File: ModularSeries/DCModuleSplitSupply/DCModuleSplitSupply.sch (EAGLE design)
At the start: 21 parts

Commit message: All PCBs now use unified library, Eagle library added
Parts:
- DCDC1: device ElectricNoodleBox2018:VRA1212ZP-6WR3 -> ElectricNoodleBox:VRA1212ZP-6WR3
- J1, J6, J7: value (none) -> 2XMOLEX; device SparkFun-Connectors:CONN_02POLAR -> ElectricNoodleBox:2XMOLEX
- J2, J3, J4, J5, J8: value (none) -> 4XMOLEX; device SparkFun-Connectors:CONN_04POLAR -> ElectricNoodleBox:4XMOLEX
- PREF1, PREF2: device ElectricNoodleBox2018:LM4040_TO92 -> ElectricNoodleBox:LM4040_TO92
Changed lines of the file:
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@@
 </classes>
 <parts>
-<part name="DCDC1" library="ElectricNoodleBox2018" deviceset="VRA1212ZP-6WR3" device="" value="+/- 12V"/>
+<part name="DCDC1" library="ElectricNoodleBox" deviceset="VRA1212ZP-6WR3" device="" value="+/- 12V"/>
 <part name="C1" library="rcl" library_urn="urn:adsk.eagle:library:334" deviceset="CPOL-EU" device="E2.5-6" package3d_urn="urn:adsk.eagle:package:23349/1" value="100µF"/>
 <part name="C2" library="rcl" library_urn="urn:adsk.eagle:library:334" deviceset="CPOL-EU" device="E2-5" package3d_urn="urn:adsk.eagle:package:23346/2" value="10µF"/>
 <part name="C3" library="rcl" library_urn="urn:adsk.eagle:library:334" deviceset="CPOL-EU" device="E2-5" package3d_urn="urn:adsk.eagle:package:23346/2" value="10µF"/>
-<part name="PREF1" library="ElectricNoodleBox2018" deviceset="LM4040_TO92" device="" value="LM4040 10V"/>
-<part name="PREF2" library="ElectricNoodleBox2018" deviceset="LM4040_TO92" device="" value="LM4040 10V"/>
+<part name="PREF1" library="ElectricNoodleBox" deviceset="LM4040_TO92" device="" value="LM4040 10V"/>
+<part name="PREF2" library="ElectricNoodleBox" deviceset="LM4040_TO92" device="" value="LM4040 10V"/>
 <part name="P+1" library="supply1" library_urn="urn:adsk.eagle:library:371" deviceset="+12V" device=""/>
 <part name="P-1" library="supply1" library_urn="urn:adsk.eagle:library:371" deviceset="-12V" device=""/>
@@
 <part name="R2" library="rcl" library_urn="urn:adsk.eagle:library:334" deviceset="R-EU_" device="0207/10" package3d_urn="urn:adsk.eagle:package:23491/2" value="4K7"/>
 <part name="AGND1" library="supply1" library_urn="urn:adsk.eagle:library:371" deviceset="AGND" device=""/>
-<part name="J1" library="SparkFun-Connectors" deviceset="CONN_02" device="POLAR"/>
-<part name="J2" library="SparkFun-Connectors" deviceset="CONN_04" device="POLAR"/>
-<part name="J3" library="SparkFun-Connectors" deviceset="CONN_04" device="POLAR"/>
-<part name="J4" library="SparkFun-Connectors" deviceset="CONN_04" device="POLAR"/>
-<part name="J5" library="SparkFun-Connectors" deviceset="CONN_04" device="POLAR"/>
-<part name="J6" library="SparkFun-Connectors" deviceset="CONN_02" device="POLAR"/>
-<part name="J7" library="SparkFun-Connectors" deviceset="CONN_02" device="POLAR"/>
-<part name="J8" library="SparkFun-Connectors" deviceset="CONN_04" device="POLAR"/>
+<part name="J1" library="ElectricNoodleBox" deviceset="2XMOLEX" device=""/>
+<part name="J2" library="ElectricNoodleBox" deviceset="4XMOLEX" device=""/>
+<part name="J3" library="ElectricNoodleBox" deviceset="4XMOLEX" device=""/>
+<part name="J4" library="ElectricNoodleBox" deviceset="4XMOLEX" device=""/>
+<part name="J5" library="ElectricNoodleBox" deviceset="4XMOLEX" device=""/>
+<part name="J6" library="ElectricNoodleBox" deviceset="2XMOLEX" device=""/>
+<part name="J7" library="ElectricNoodleBox" deviceset="2XMOLEX" device=""/>
+<part name="J8" library="ElectricNoodleBox" deviceset="4XMOLEX" device=""/>
 <part name="P-2" library="supply1" library_urn="urn:adsk.eagle:library:371" deviceset="-12V" device=""/>
 <part name="P+2" library="supply1" library_urn="urn:adsk.eagle:library:371" deviceset="+12V" device=""/>
@@
 </instance>
 <instance part="J1" gate="G$1" x="25.4" y="45.72" smashed="yes" rot="MR180">
-<attribute name="VALUE" x="22.86" y="50.546" size="1.778" layer="96" font="vector" rot="MR180"/>
 <attribute name="NAME" x="22.86" y="40.132" size="1.778" layer="95" font="vector" rot="MR180"/>
 </instance>
 <instance part="J2" gate="G$1" x="121.92" y="73.66" smashed="yes" rot="MR180">
-<attribute name="VALUE" x="116.84" y="81.026" size="1.778" layer="96" font="vector" rot="MR180"/>
 <attribute name="NAME" x="116.84" y="65.532" size="1.778" layer="95" font="vector" rot="MR180"/>
 </instance>
 <instance part="J3" gate="G$1" x="121.92" y="58.42" smashed="yes" rot="MR180">
-<attribute name="VALUE" x="116.84" y="65.786" size="1.778" layer="96" font="vector" rot="MR180"/>
 <attribute name="NAME" x="116.84" y="50.292" size="1.778" layer="95" font="vector" rot="MR180"/>
 </instance>
 <instance part="J4" gate="G$1" x="121.92" y="43.18" smashed="yes" rot="MR180">
-<attribute name="VALUE" x="116.84" y="50.546" size="1.778" layer="96" font="vector" rot="MR180"/>
 <attribute name="NAME" x="116.84" y="35.052" size="1.778" layer="95" font="vector" rot="MR180"/>
 </instance>
 <instance part="J5" gate="G$1" x="121.92" y="27.94" smashed="yes" rot="MR180">
-<attribute name="VALUE" x="116.84" y="35.306" size="1.778" layer="96" font="vector" rot="MR180"/>
 <attribute name="NAME" x="116.84" y="19.812" size="1.778" layer="95" font="vector" rot="MR180"/>
 </instance>
 <instance part="J6" gate="G$1" x="154.94" y="48.26" smashed="yes" rot="R180">
-<attribute name="VALUE" x="157.48" y="53.086" size="1.778" layer="96" font="vector" rot="R180"/>
 <attribute name="NAME" x="157.48" y="42.672" size="1.778" layer="95" font="vector" rot="R180"/>
 </instance>
 <instance part="J7" gate="G$1" x="154.94" y="35.56" smashed="yes" rot="R180">
-<attribute name="VALUE" x="157.48" y="40.386" size="1.778" layer="96" font="vector" rot="R180"/>
 <attribute name="NAME" x="157.48" y="29.972" size="1.778" layer="95" font="vector" rot="R180"/>
 </instance>
 <instance part="J8" gate="G$1" x="121.92" y="12.7" smashed="yes" rot="MR180">
-<attribute name="VALUE" x="116.84" y="20.066" size="1.778" layer="96" font="vector" rot="MR180"/>
 <attribute name="NAME" x="116.84" y="4.572" size="1.778" layer="95" font="vector" rot="MR180"/>
 </instance>

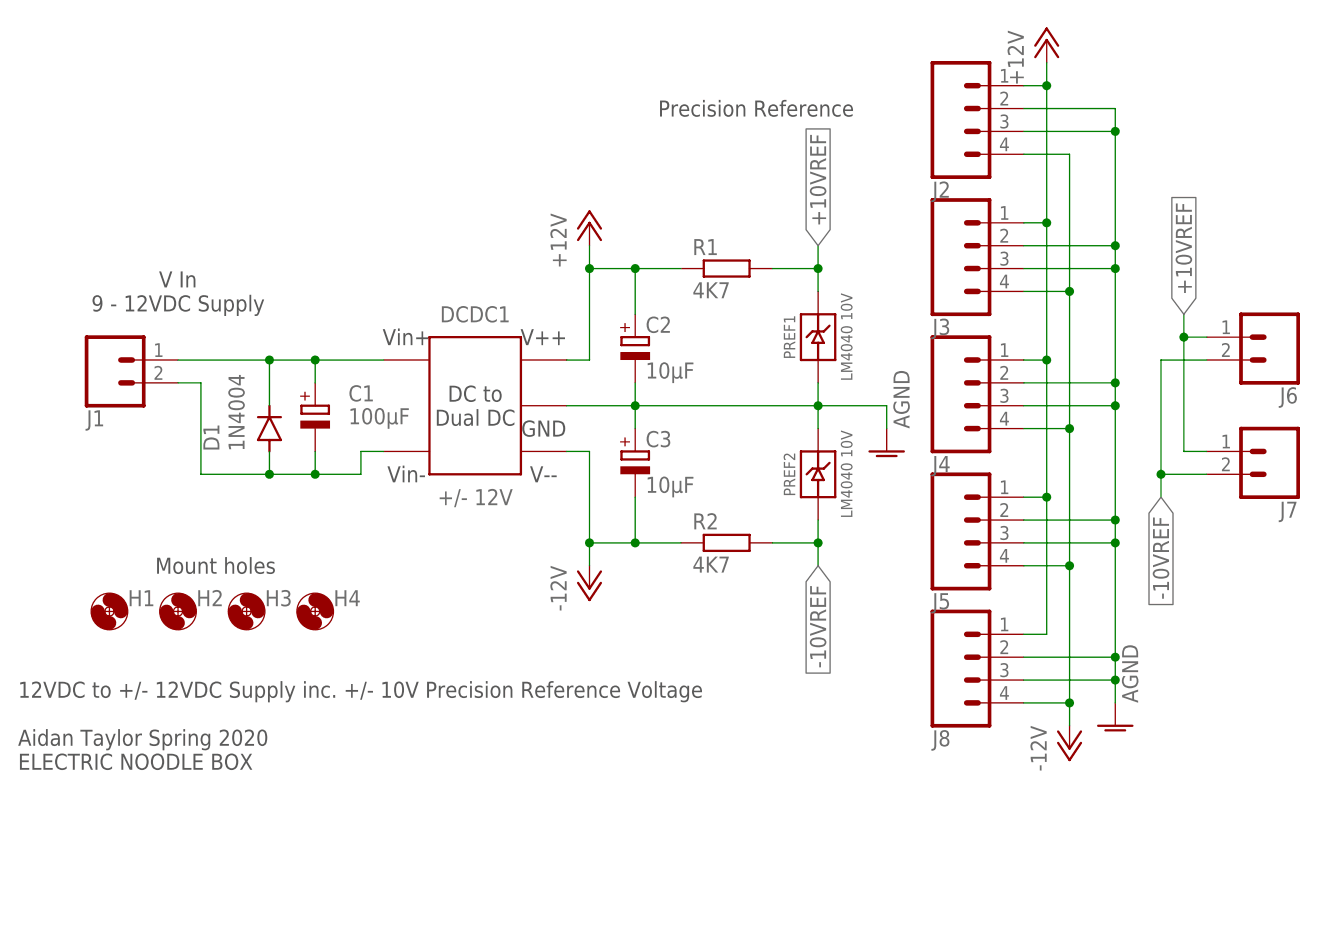
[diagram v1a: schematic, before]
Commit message: Updates to Prism, VCA, PSU and Prism BOM added
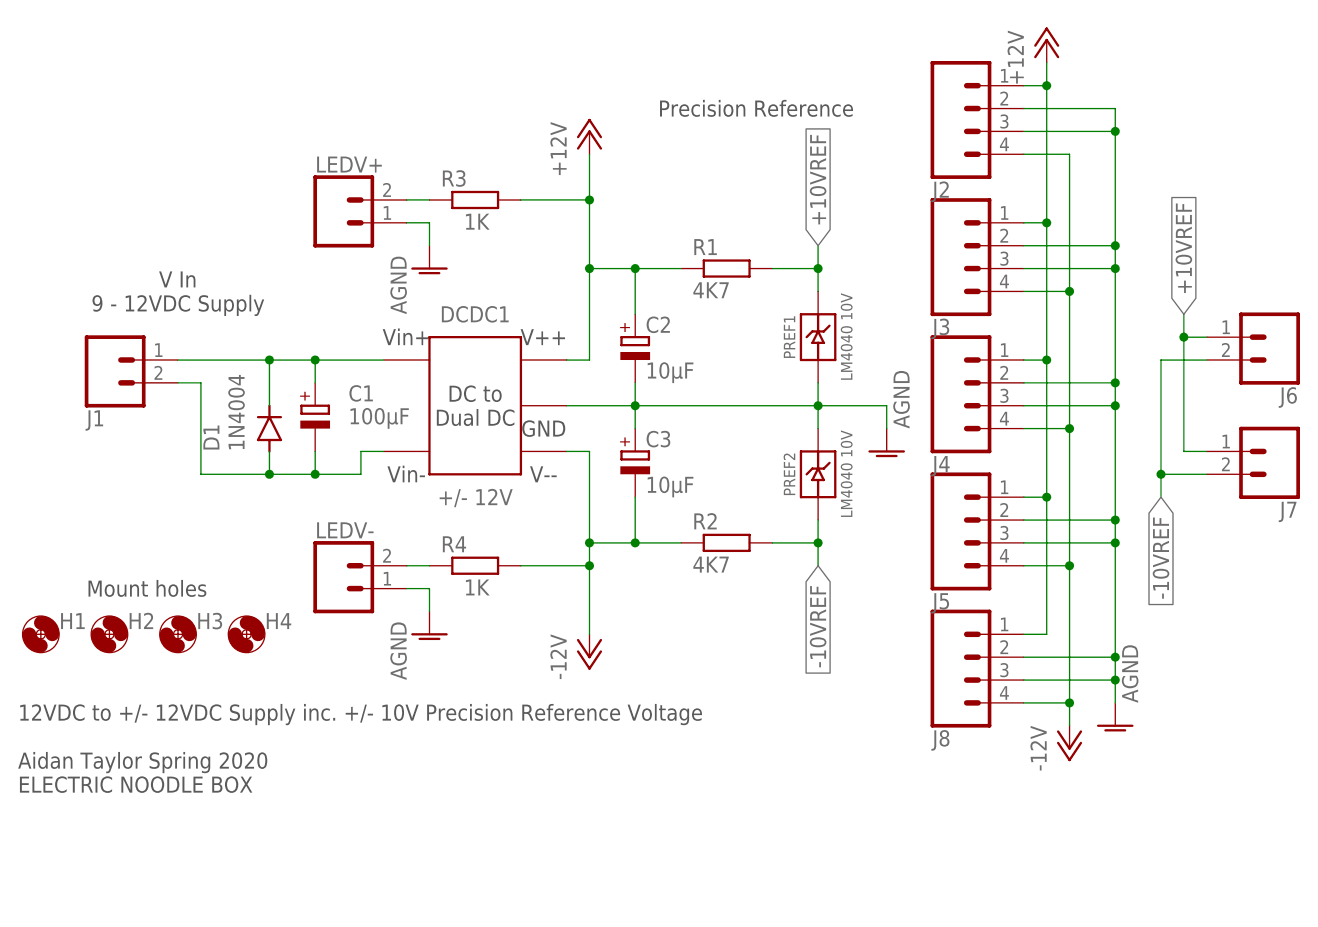
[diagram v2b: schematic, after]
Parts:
- added LEDV+, LEDV-: 2XWIREPAD, ElectricNoodleBox:2XWIREPAD
- added R3, R4: 1K, rcl:R-EU_0207/10
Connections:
- new net N$2: LEDV+.2, R3.1
- new net N$3: LEDV-.2, R4.1
- net +12V: now also R3.2
- net -12V: now also R4.2
- net AGND: now also LEDV+.1, LEDV-.1
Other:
- moved on the sheet: H1, H2, H3, H4
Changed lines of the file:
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@@
 <part name="H3" library="holes" library_urn="urn:adsk.eagle:library:237" deviceset="MOUNT-HOLE" device="3.2" package3d_urn="urn:adsk.eagle:package:14275/1"/>
 <part name="H4" library="holes" library_urn="urn:adsk.eagle:library:237" deviceset="MOUNT-HOLE" device="3.2" package3d_urn="urn:adsk.eagle:package:14275/1"/>
+<part name="LEDV+" library="ElectricNoodleBox" deviceset="2XWIREPAD" device=""/>
+<part name="LEDV-" library="ElectricNoodleBox" deviceset="2XWIREPAD" device=""/>
+<part name="R3" library="rcl" library_urn="urn:adsk.eagle:library:334" deviceset="R-EU_" device="0207/10" package3d_urn="urn:adsk.eagle:package:23491/2" value="1K"/>
+<part name="AGND3" library="supply1" library_urn="urn:adsk.eagle:library:371" deviceset="AGND" device=""/>
+<part name="AGND4" library="supply1" library_urn="urn:adsk.eagle:library:371" deviceset="AGND" device=""/>
+<part name="R4" library="rcl" library_urn="urn:adsk.eagle:library:334" deviceset="R-EU_" device="0207/10" package3d_urn="urn:adsk.eagle:package:23491/2" value="1K"/>
 </parts>
 <sheets>
@@
 <text x="33.02" y="53.34" size="1.778" layer="97" align="center">V In
 9 - 12VDC Supply</text>
-<text x="15.24" y="5.08" size="1.778" layer="97" align="center-left">12VDC to +/- 12VDC Supply inc. +/- 10V Precision Reference Voltage
+<text x="15.24" y="2.54" size="1.778" layer="97" align="center-left">12VDC to +/- 12VDC Supply inc. +/- 10V Precision Reference Voltage
 Aidan Taylor Spring 2020
 ELECTRIC NOODLE BOX</text>
 <text x="86.36" y="73.66" size="1.778" layer="97" align="center-left">Precision Reference</text>
-<text x="30.48" y="22.86" size="1.778" layer="97" align="center-left">Mount holes</text>
+<text x="22.86" y="20.32" size="1.778" layer="97" align="center-left">Mount holes</text>
 </plain>
 <instances>
@@
 <attribute name="VALUE" x="107.315" y="33.02" size="1.27" layer="96" rot="R90" align="center"/>
 </instance>
-<instance part="P+1" gate="1" x="78.74" y="60.96" smashed="yes">
-<attribute name="VALUE" x="76.2" y="55.88" size="1.778" layer="96" rot="R90"/>
-</instance>
-<instance part="P-1" gate="1" x="78.74" y="20.32" smashed="yes">
-<attribute name="VALUE" x="76.2" y="17.78" size="1.778" layer="96" rot="R90"/>
+<instance part="P+1" gate="1" x="78.74" y="71.12" smashed="yes">
+<attribute name="VALUE" x="76.2" y="66.04" size="1.778" layer="96" rot="R90"/>
+</instance>
+<instance part="P-1" gate="1" x="78.74" y="12.7" smashed="yes">
+<attribute name="VALUE" x="76.2" y="10.16" size="1.778" layer="96" rot="R90"/>
 </instance>
 <instance part="R1" gate="G$1" x="93.98" y="55.88" smashed="yes">
@@
 <attribute name="VALUE" x="40.4114" y="35.56" size="1.778" layer="96" rot="R90"/>
 </instance>
-<instance part="H1" gate="G$1" x="25.4" y="17.78" smashed="yes">
-<attribute name="NAME" x="27.432" y="18.3642" size="1.778" layer="95"/>
-</instance>
-<instance part="H2" gate="G$1" x="33.02" y="17.78" smashed="yes">
-<attribute name="NAME" x="35.052" y="18.3642" size="1.778" layer="95"/>
-</instance>
-<instance part="H3" gate="G$1" x="40.64" y="17.78" smashed="yes">
-<attribute name="NAME" x="42.672" y="18.3642" size="1.778" layer="95"/>
-</instance>
-<instance part="H4" gate="G$1" x="48.26" y="17.78" smashed="yes">
-<attribute name="NAME" x="50.292" y="18.3642" size="1.778" layer="95"/>
+<instance part="H1" gate="G$1" x="17.78" y="15.24" smashed="yes">
+<attribute name="NAME" x="19.812" y="15.8242" size="1.778" layer="95"/>
+</instance>
+<instance part="H2" gate="G$1" x="25.4" y="15.24" smashed="yes">
+<attribute name="NAME" x="27.432" y="15.8242" size="1.778" layer="95"/>
+</instance>
+<instance part="H3" gate="G$1" x="33.02" y="15.24" smashed="yes">
+<attribute name="NAME" x="35.052" y="15.8242" size="1.778" layer="95"/>
+</instance>
+<instance part="H4" gate="G$1" x="40.64" y="15.24" smashed="yes">
+<attribute name="NAME" x="42.672" y="15.8242" size="1.778" layer="95"/>
+</instance>
+<instance part="LEDV+" gate="G$1" x="50.8" y="60.96" smashed="yes">
+<attribute name="NAME" x="48.26" y="66.548" size="1.778" layer="95" font="vector"/>
+</instance>
+<instance part="LEDV-" gate="G$1" x="50.8" y="20.32" smashed="yes">
+<attribute name="NAME" x="48.26" y="25.908" size="1.778" layer="95" font="vector"/>
+</instance>
+<instance part="R3" gate="G$1" x="66.04" y="63.5" smashed="yes">
+<attribute name="NAME" x="62.23" y="64.9986" size="1.778" layer="95"/>
+<attribute name="VALUE" x="64.77" y="60.198" size="1.778" layer="96"/>
+</instance>
+<instance part="AGND3" gate="VR1" x="60.96" y="55.88" smashed="yes">
+<attribute name="VALUE" x="58.42" y="50.8" size="1.778" layer="96" rot="R90"/>
+</instance>
+<instance part="AGND4" gate="VR1" x="60.96" y="15.24" smashed="yes">
+<attribute name="VALUE" x="58.42" y="10.16" size="1.778" layer="96" rot="R90"/>
+</instance>
+<instance part="R4" gate="G$1" x="66.04" y="22.86" smashed="yes">
+<attribute name="NAME" x="62.23" y="24.3586" size="1.778" layer="95"/>
+<attribute name="VALUE" x="64.77" y="19.558" size="1.778" layer="96"/>
 </instance>
 </instances>
@@
 <wire x1="78.74" y1="45.72" x2="78.74" y2="55.88" width="0.1524" layer="91"/>
 <pinref part="R1" gate="G$1" pin="1"/>
-<wire x1="78.74" y1="55.88" x2="78.74" y2="58.42" width="0.1524" layer="91"/>
+<wire x1="78.74" y1="55.88" x2="78.74" y2="63.5" width="0.1524" layer="91"/>
+<wire x1="78.74" y1="63.5" x2="78.74" y2="68.58" width="0.1524" layer="91"/>
 <wire x1="78.74" y1="55.88" x2="83.82" y2="55.88" width="0.1524" layer="91"/>
 <junction x="78.74" y="55.88"/>
@@
 <wire x1="83.82" y1="55.88" x2="83.82" y2="50.8" width="0.1524" layer="91"/>
 <junction x="83.82" y="55.88"/>
+<pinref part="R3" gate="G$1" pin="2"/>
+<wire x1="71.12" y1="63.5" x2="78.74" y2="63.5" width="0.1524" layer="91"/>
+<junction x="78.74" y="63.5"/>
 </segment>
 <segment>
@@
 <pinref part="C3" gate="G$1" pin="-"/>
 <wire x1="78.74" y1="25.4" x2="78.74" y2="22.86" width="0.1524" layer="91"/>
+<wire x1="78.74" y1="22.86" x2="78.74" y2="15.24" width="0.1524" layer="91"/>
 <wire x1="83.82" y1="30.48" x2="83.82" y2="25.4" width="0.1524" layer="91"/>
 <pinref part="R2" gate="G$1" pin="1"/>
@@
 <junction x="78.74" y="25.4"/>
 <junction x="83.82" y="25.4"/>
+<pinref part="R4" gate="G$1" pin="2"/>
+<wire x1="71.12" y1="22.86" x2="78.74" y2="22.86" width="0.1524" layer="91"/>
+<junction x="78.74" y="22.86"/>
 </segment>
 <segment>
@@
 <junction x="137.16" y="10.16"/>
 </segment>
-</net>
+<segment>
+<pinref part="LEDV+" gate="G$1" pin="1"/>
+<wire x1="58.42" y1="60.96" x2="60.96" y2="60.96" width="0.1524" layer="91"/>
+<pinref part="AGND3" gate="VR1" pin="AGND"/>
+<wire x1="60.96" y1="60.96" x2="60.96" y2="58.42" width="0.1524" layer="91"/>
+</segment>
+<segment>
+<pinref part="LEDV-" gate="G$1" pin="1"/>
+<wire x1="58.42" y1="20.32" x2="60.96" y2="20.32" width="0.1524" layer="91"/>
+<pinref part="AGND4" gate="VR1" pin="AGND"/>
+<wire x1="60.96" y1="20.32" x2="60.96" y2="17.78" width="0.1524" layer="91"/>
+</segment>
+</net>
+<net name="N$2" class="0">
+<segment>
+<pinref part="LEDV+" gate="G$1" pin="2"/>
+<pinref part="R3" gate="G$1" pin="1"/>
+<wire x1="58.42" y1="63.5" x2="60.96" y2="63.5" width="0.1524" layer="91"/>
+</segment>
+</net>
+<net name="N$3" class="0">
+<segment>
+<pinref part="LEDV-" gate="G$1" pin="2"/>
+<pinref part="R4" gate="G$1" pin="1"/>
+<wire x1="58.42" y1="22.86" x2="60.96" y2="22.86" width="0.1524" layer="91"/>
+</segment>
+</net>

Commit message: Portals files updated, schematic exports and images included
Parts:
- added LINK: 2XWIREPAD, ElectricNoodleBox:2XWIREPAD
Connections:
- net AGND: now also LINK.1, LINK.2
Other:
- note added: "Ground link for Banana systems"
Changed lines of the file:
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@@
 <part name="AGND4" library="supply1" library_urn="urn:adsk.eagle:library:371" deviceset="AGND" device=""/>
 <part name="R4" library="rcl" library_urn="urn:adsk.eagle:library:334" deviceset="R-EU_" device="0207/10" package3d_urn="urn:adsk.eagle:package:23491/2" value="1K"/>
+<part name="LINK" library="ElectricNoodleBox" deviceset="2XWIREPAD" device=""/>
+<part name="AGND5" library="supply1" library_urn="urn:adsk.eagle:library:371" deviceset="AGND" device=""/>
 </parts>
 <sheets>
@@
 <text x="86.36" y="73.66" size="1.778" layer="97" align="center-left">Precision Reference</text>
 <text x="22.86" y="20.32" size="1.778" layer="97" align="center-left">Mount holes</text>
+<text x="22.86" y="76.2" size="1.778" layer="91">Ground link
+for Banana systems</text>
 </plain>
 <instances>
@@
 <attribute name="NAME" x="62.23" y="24.3586" size="1.778" layer="95"/>
 <attribute name="VALUE" x="64.77" y="19.558" size="1.778" layer="96"/>
+</instance>
+<instance part="LINK" gate="G$1" x="25.4" y="66.04" smashed="yes">
+<attribute name="NAME" x="22.86" y="71.628" size="1.778" layer="95" font="vector"/>
+</instance>
+<instance part="AGND5" gate="VR1" x="35.56" y="60.96" smashed="yes">
+<attribute name="VALUE" x="38.1" y="63.5" size="1.778" layer="96" rot="R90"/>
 </instance>
 </instances>
@@
 <wire x1="60.96" y1="20.32" x2="60.96" y2="17.78" width="0.1524" layer="91"/>
 </segment>
-</net>
+<segment>
+<pinref part="LINK" gate="G$1" pin="1"/>
+<wire x1="33.02" y1="66.04" x2="35.56" y2="66.04" width="0.1524" layer="91"/>
+<pinref part="AGND5" gate="VR1" pin="AGND"/>
+<wire x1="35.56" y1="66.04" x2="35.56" y2="63.5" width="0.1524" layer="91"/>
+<pinref part="LINK" gate="G$1" pin="2"/>
+<wire x1="33.02" y1="68.58" x2="35.56" y2="68.58" width="0.1524" layer="91"/>
+<wire x1="35.56" y1="68.58" x2="35.56" y2="66.04" width="0.1524" layer="91"/>
+<junction x="35.56" y="66.04"/>
+</segment>
+</net>
